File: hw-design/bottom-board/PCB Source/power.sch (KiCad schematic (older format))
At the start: 29 parts, among them J1 Power Jack, J2 HMI_POWER, U2 LD1117S50TR_SOT223

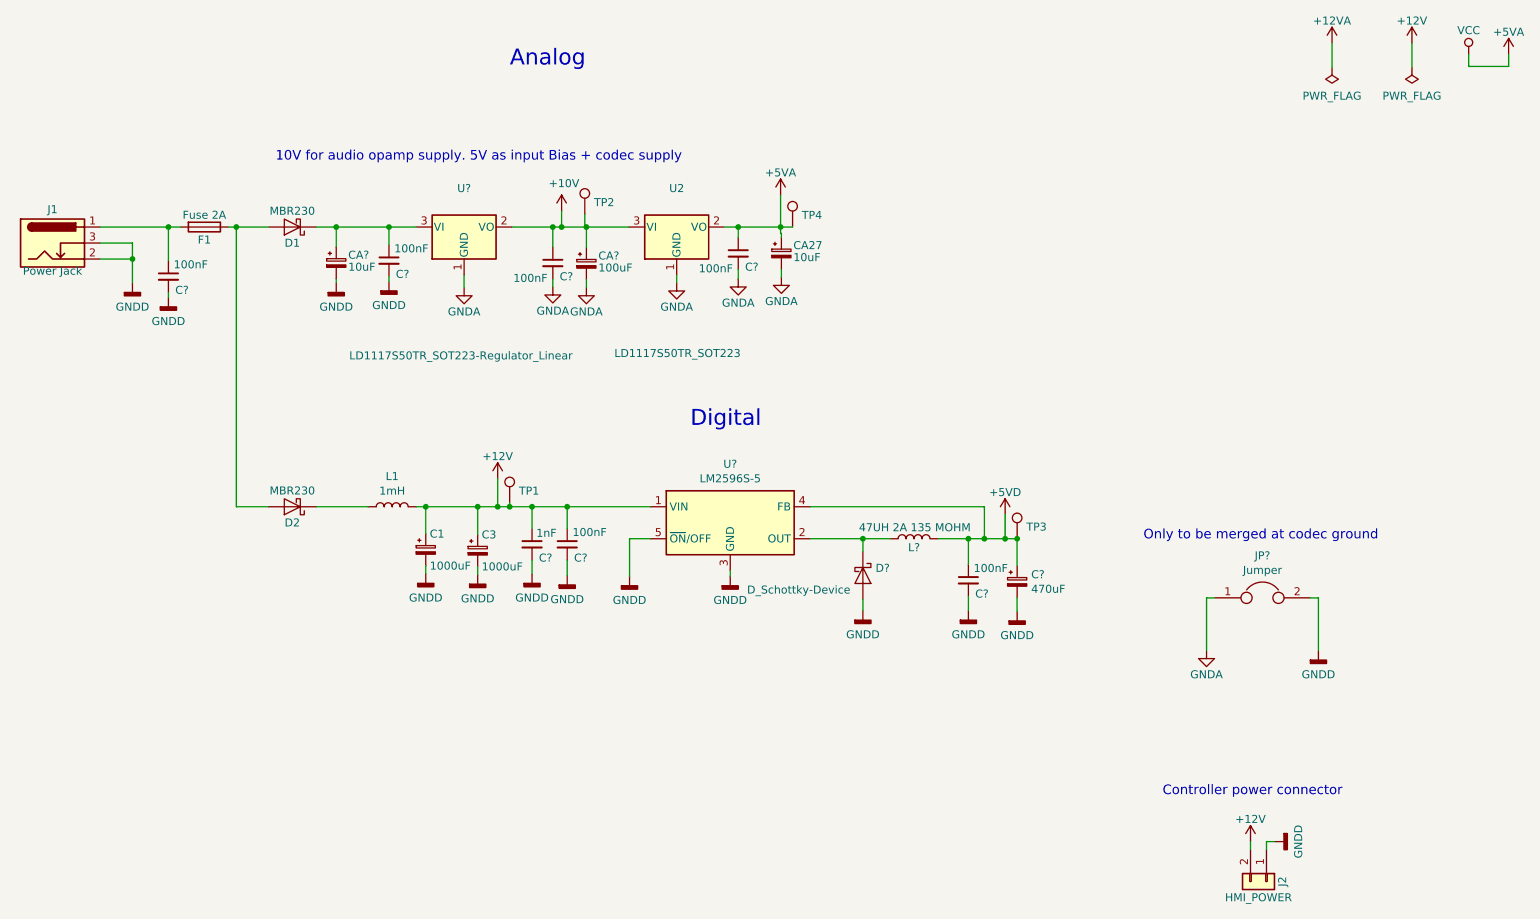
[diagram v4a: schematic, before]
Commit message: place new power curcuit on the PCB
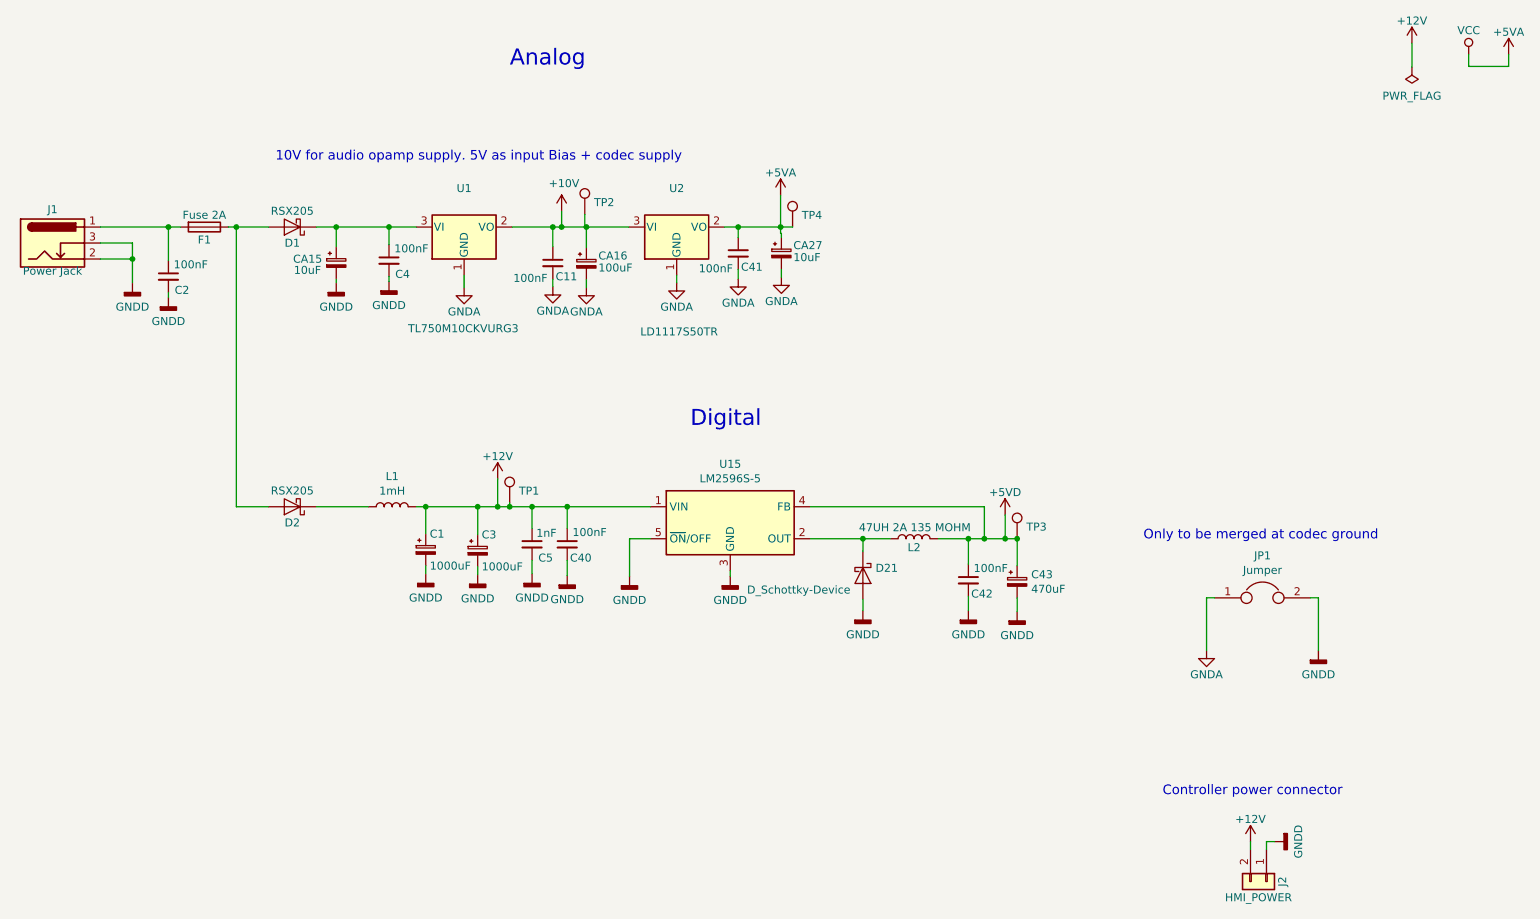
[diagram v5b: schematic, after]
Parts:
- D1, D2: value MBR230 -> RSX205; MPN MBR230LSFT1G -> RSX205LAM30TR
- D21: renamed from D?; footprint (none) -> Diode_SMD:D_MELF; MPN (none) -> TSSA3U45 R3G
- JP1: renamed from JP?; footprint (none) -> Jumper:SolderJumper-2_P1.3mm_Bridged2Bar_RoundedPad1.0x1.5mm
- U1: renamed from U?; value LD1117S50TR_SOT223-Regulator_Linear -> TL750M10CKVURG3; MPN (none) -> TL750M10CKVURG3
- U15: renamed from U?; MPN (none) -> TS2596CM550 RNG
- U2: value LD1117S50TR_SOT223 -> LD1117S50TR
- gave numbers to parts that had none: 11

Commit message: route codec to new SoM
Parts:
- U1: footprint Package_TO_SOT_SMD:SOT-223-3_TabPin2 -> Package_TO_SOT_SMD:TO-252-3_TabPin2
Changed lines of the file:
@@
 F 0 "U1" H 4425 2192 50  0000 C CNN
 F 1 "TL750M10CKVURG3" H 4420 1315 50  0000 C CNN
-F 2 "Package_TO_SOT_SMD:SOT-223-3_TabPin2" H 4425 2150 50  0001 C CNN
+F 2 "Package_TO_SOT_SMD:TO-252-3_TabPin2" H 4425 2150 50  0001 C CNN
 F 3 "" H 4525 1700 50  0001 C CNN
 F 4 "TL750M10CKVURG3" H 4425 1950 50  0001 C CNN "MPN"
